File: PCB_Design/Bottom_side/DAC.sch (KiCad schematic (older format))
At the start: 5 parts, among them U4 MCP4728

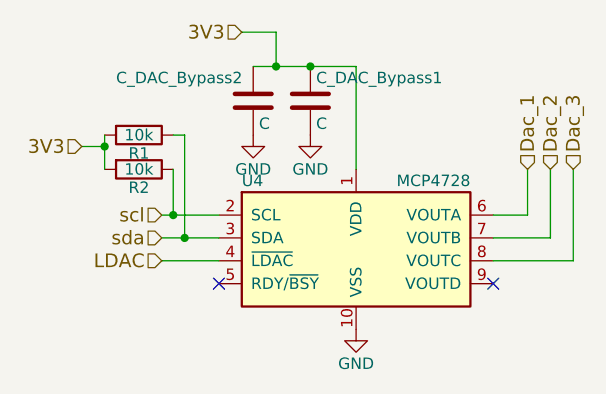
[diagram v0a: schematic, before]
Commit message: PCB bottom layer populated
PCB bottom layer populated, and waiting for top layer to be merged.
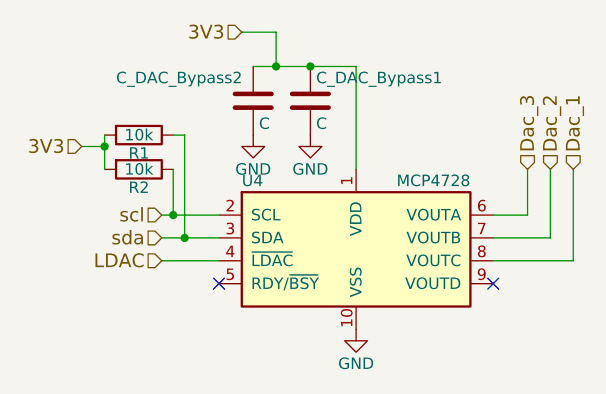
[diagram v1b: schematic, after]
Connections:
- net Dac_1: now also U4.8 (VOUTC); no longer U4.6 (VOUTA)
- net Dac_3: now also U4.6 (VOUTA); no longer U4.8 (VOUTC)
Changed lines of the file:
@@
 LIBS:contrib
 LIBS:valves
-LIBS:Custom_Library
 LIBS:Bottom_side-cache
 EELAYER 25 0
@@
 $Descr A4 11693 8268
 encoding utf-8
-Sheet 11 25
+Sheet 11 26
 Title ""
 Date ""
@@
 	3650 2500 4100 2500
 $Comp
-L GND #PWR041
+L GND #PWR047
 U 1 1 5A57FCC2
 P 3900 2800
-F 0 "#PWR041" H 3900 2550 50  0001 C CNN
+F 0 "#PWR047" H 3900 2550 50  0001 C CNN
 F 1 "GND" H 3900 2650 50  0000 C CNN
 F 2 "" H 3900 2800 50  0001 C CNN
@@
 Connection ~ 3900 2500
 $Comp
-L GND #PWR042
+L GND #PWR048
 U 1 1 5A57FCFF
 P 3650 2800
-F 0 "#PWR042" H 3650 2550 50  0001 C CNN
+F 0 "#PWR048" H 3650 2550 50  0001 C CNN
 F 1 "GND" H 3650 2650 50  0000 C CNN
 F 2 "" H 3650 2800 50  0001 C CNN
@@
 NoConn ~ 4700 3450
 $Comp
-L GND #PWR043
+L GND #PWR049
 U 1 1 5A57FDA0
 P 4100 3650
-F 0 "#PWR043" H 4100 3400 50  0001 C CNN
+F 0 "#PWR049" H 4100 3400 50  0001 C CNN
 F 1 "GND" H 4100 3500 50  0000 C CNN
 F 2 "" H 4100 3650 50  0001 C CNN
@@
 	1    0    0    -1
 $EndComp
-Text HLabel 4850 2950 1    60   Input ~ 0
+Text HLabel 5050 2950 1    60   Input ~ 0
 Dac_1
 Text HLabel 4950 2950 1    60   Input ~ 0
 Dac_2
-Text HLabel 5050 2950 1    60   Input ~ 0
+Text HLabel 4850 2950 1    60   Input ~ 0
 Dac_3
 Text HLabel 3250 3150 0    60   Input ~ 0

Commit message: Updated PCB structure tree
Full_PCB now includes bottom and top layer hierarchical sheets
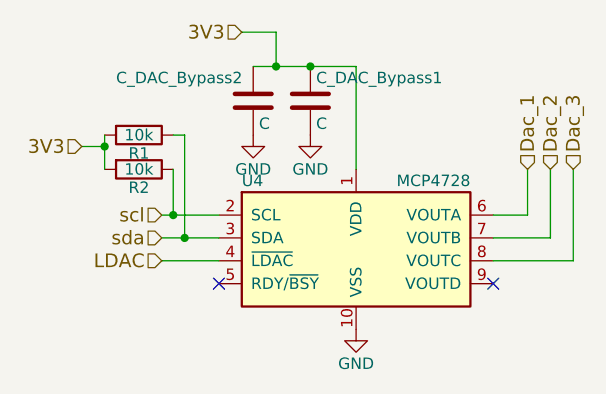
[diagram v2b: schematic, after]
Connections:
- net Dac_1: now also U4.6 (VOUTA); no longer U4.8 (VOUTC)
- net Dac_3: now also U4.8 (VOUTC); no longer U4.6 (VOUTA)
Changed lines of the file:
@@
 LIBS:power
 LIBS:device
-LIBS:switches
-LIBS:relays
-LIBS:motors
 LIBS:transistors
 LIBS:conn
@@
 LIBS:contrib
 LIBS:valves
-LIBS:Bottom_side-cache
+LIBS:Full_PCB-cache
 EELAYER 25 0
 EELAYER END
@@
 	3650 2500 4100 2500
 $Comp
-L GND #PWR047
+L GND #PWR041
 U 1 1 5A57FCC2
 P 3900 2800
-F 0 "#PWR047" H 3900 2550 50  0001 C CNN
+F 0 "#PWR041" H 3900 2550 50  0001 C CNN
 F 1 "GND" H 3900 2650 50  0000 C CNN
 F 2 "" H 3900 2800 50  0001 C CNN
@@
 Connection ~ 3900 2500
 $Comp
-L GND #PWR048
+L GND #PWR042
 U 1 1 5A57FCFF
 P 3650 2800
-F 0 "#PWR048" H 3650 2550 50  0001 C CNN
+F 0 "#PWR042" H 3650 2550 50  0001 C CNN
 F 1 "GND" H 3650 2650 50  0000 C CNN
 F 2 "" H 3650 2800 50  0001 C CNN
@@
 NoConn ~ 4700 3450
 $Comp
-L GND #PWR049
+L GND #PWR043
 U 1 1 5A57FDA0
 P 4100 3650
-F 0 "#PWR049" H 4100 3400 50  0001 C CNN
+F 0 "#PWR043" H 4100 3400 50  0001 C CNN
 F 1 "GND" H 4100 3500 50  0000 C CNN
 F 2 "" H 4100 3650 50  0001 C CNN
@@
 	1    0    0    -1
 $EndComp
-Text HLabel 5050 2950 1    60   Input ~ 0
+Text HLabel 4850 2950 1    60   Input ~ 0
 Dac_1
 Text HLabel 4950 2950 1    60   Input ~ 0
 Dac_2
-Text HLabel 4850 2950 1    60   Input ~ 0
+Text HLabel 5050 2950 1    60   Input ~ 0
 Dac_3
 Text HLabel 3250 3150 0    60   Input ~ 0
